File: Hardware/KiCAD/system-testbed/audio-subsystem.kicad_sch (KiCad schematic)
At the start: 29 parts, among them J4 Conn_01x08_Pin, SW2 SW_SPDT, U1 MAX98357A

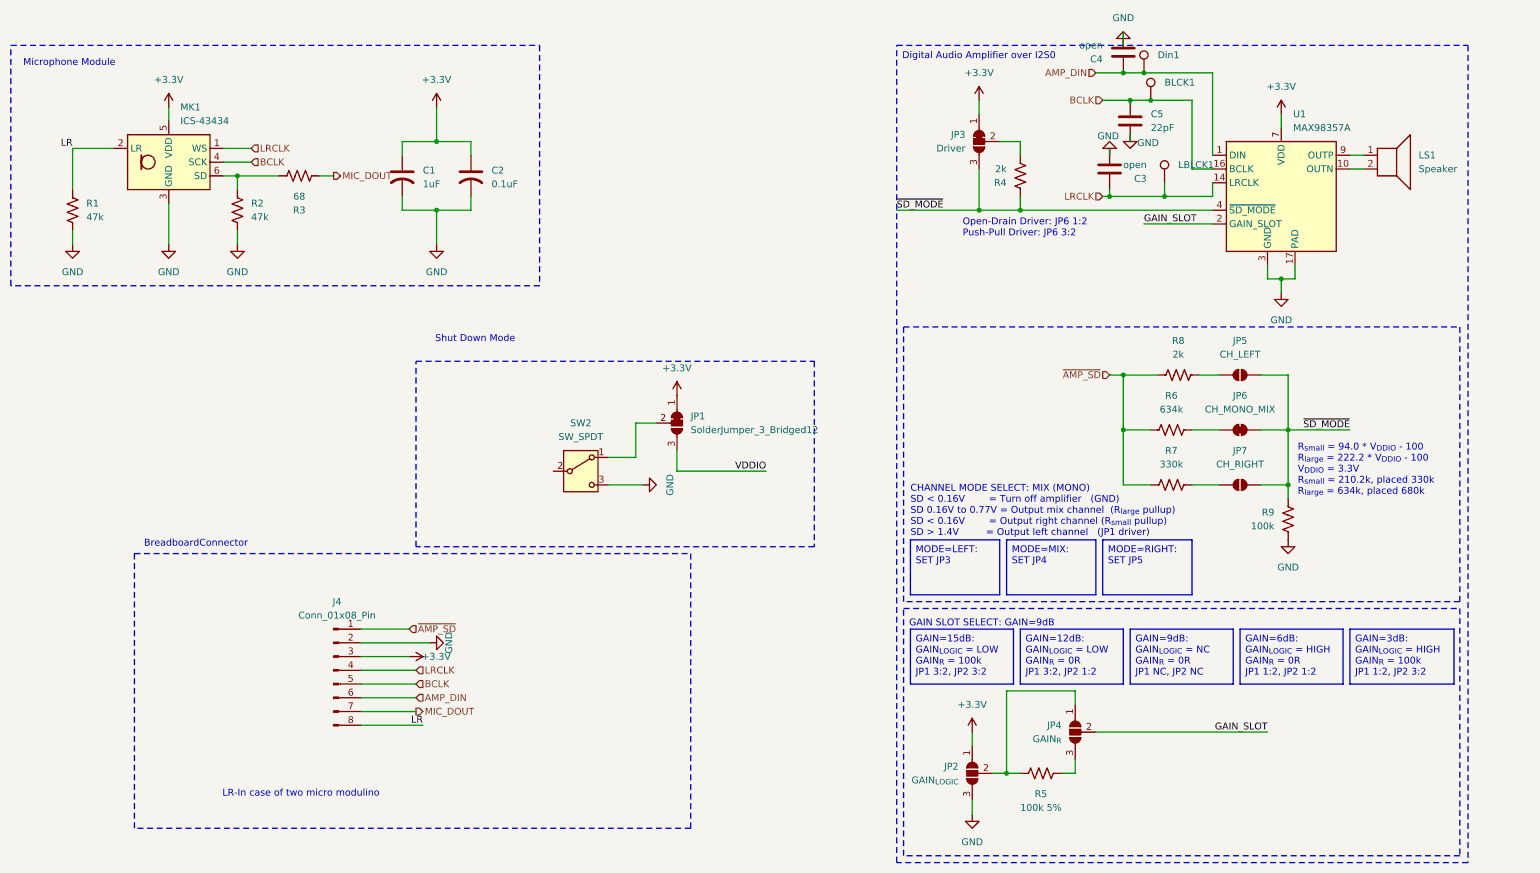
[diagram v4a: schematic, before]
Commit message: fix: recover audio schematic #70
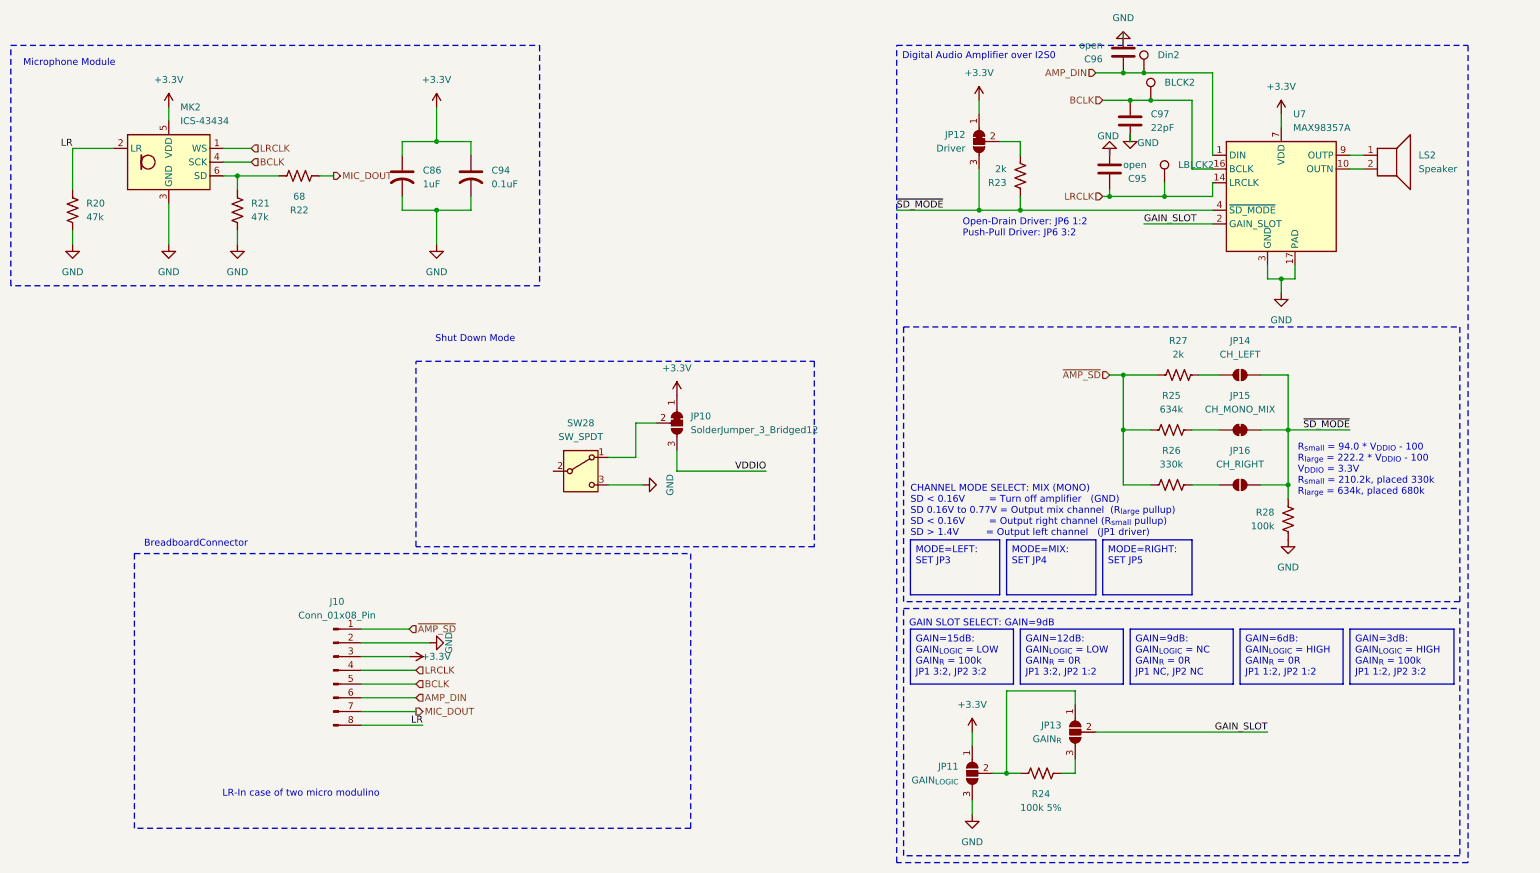
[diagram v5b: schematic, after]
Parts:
- renumbered BLCK1 to BLCK2, C1 to C86, C2 to C94, C3 to C95, C4 to C96, C5 to C97, Din1 to Din2, J4 to J10, JP1 to JP10, JP2 to JP11, JP3 to JP12, JP4 to JP13, JP5 to JP14, JP6 to JP15, JP7 to JP16, LBLCK1 to LBLCK2, LS1 to LS2, MK1 to MK2, R1 to R20, R2 to R21, R3 to R22, R4 to R23, R5 to R24, R6 to R25, R7 to R26, R8 to R27, R9 to R28, SW2 to SW28, U1 to U7
